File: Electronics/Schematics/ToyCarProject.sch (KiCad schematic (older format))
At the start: 24 parts

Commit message: Project Schematics update
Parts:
- added P?: MSP430G2553, symbol MSP430G2553
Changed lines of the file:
@@
-EESchema Schematic File Version 2  date 25/02/2013 10:51:28
+EESchema Schematic File Version 2  date 2/28/2013 14:46:19
 LIBS:power
 LIBS:device
@@
 LIBS:contrib
 LIBS:valves
-EELAYER 43  0
+LIBS:ToyCarProject-cache
+EELAYER 27 0
 EELAYER END
-$Descr A4 11700 8267
+$Descr A4 11693 8268
 encoding utf-8
 Sheet 1 1
 Title ""
-Date "25 feb 2013"
+Date "28 feb 2013"
 Rev ""
 Comp ""
@@
 F 0 "V?" H 4150 1450 50  0000 L CNN
 F 1 "BAT" H 4150 1250 50  0000 L CNN
+F 2 "" H 4100 1350 60  0001 C CNN
+F 3 "" H 4100 1350 60  0001 C CNN
 	1    4100 1350
 	1    0    0    -1
@@
 F 0 "U?" H 4950 1104 60  0000 C CNN
 F 1 "LD1117S33" H 4800 1500 60  0000 C CNN
+F 2 "" H 4800 1300 60  0001 C CNN
+F 3 "" H 4800 1300 60  0001 C CNN
 	1    4800 1300
 	1    0    0    -1
@@
 F 0 "R?" V 2830 1800 50  0000 C CNN
 F 1 "470" V 2750 1800 50  0000 C CNN
+F 2 "" H 2750 1800 60  0001 C CNN
+F 3 "" H 2750 1800 60  0001 C CNN
 	1    2750 1800
 	-1   0    0    1
@@
 F 0 "R?" V 2480 1800 50  0000 C CNN
 F 1 "470" V 2400 1800 50  0000 C CNN
+F 2 "" H 2400 1800 60  0001 C CNN
+F 3 "" H 2400 1800 60  0001 C CNN
 	1    2400 1800
 	-1   0    0    1
@@
 F 0 "R?" V 2130 1800 50  0000 C CNN
 F 1 "470" V 2050 1800 50  0000 C CNN
+F 2 "" H 2050 1800 60  0001 C CNN
+F 3 "" H 2050 1800 60  0001 C CNN
 	1    2050 1800
 	-1   0    0    1
@@
 F 0 "D?" H 2750 1450 50  0000 C CNN
 F 1 "Mbed LED" H 2750 1250 50  0000 C CNN
+F 2 "" H 2750 1350 60  0001 C CNN
+F 3 "" H 2750 1350 60  0001 C CNN
 	1    2750 1350
 	0    -1   -1   0
@@
 F 0 "D?" H 2400 1450 50  0000 C CNN
 F 1 "Mbed LED" H 2400 1250 50  0000 C CNN
+F 2 "" H 2400 1350 60  0001 C CNN
+F 3 "" H 2400 1350 60  0001 C CNN
 	1    2400 1350
 	0    -1   -1   0
@@
 F 0 "D?" H 2050 1450 50  0000 C CNN
 F 1 "Mbed LED" H 2050 1250 50  0000 C CNN
+F 2 "" H 2050 1350 60  0001 C CNN
+F 3 "" H 2050 1350 60  0001 C CNN
 	1    2050 1350
 	0    -1   -1   0
@@
 F 0 "L?" V 9750 1400 40  0000 C CNN
 F 1 "INDUCTOR" V 9900 1400 40  0000 C CNN
+F 2 "" H 9800 1400 60  0001 C CNN
+F 3 "" H 9800 1400 60  0001 C CNN
 	1    9800 1400
 	0    -1   -1   0
@@
 F 0 "L?" V 9150 1400 40  0000 C CNN
 F 1 "INDUCTOR" V 9300 1400 40  0000 C CNN
+F 2 "" H 9200 1400 60  0001 C CNN
+F 3 "" H 9200 1400 60  0001 C CNN
 	1    9200 1400
 	0    -1   -1   0
@@
 F 0 "#PWR?" H 9500 1350 20  0001 C CNN
 F 1 "+BAT_CAR" H 9500 1500 30  0000 C CNN
+F 2 "" H 9500 1400 60  0001 C CNN
+F 3 "" H 9500 1400 60  0001 C CNN
 	1    9500 1400
 	1    0    0    -1
@@
 F 0 "Q?" H 8800 1450 50  0000 R CNN
 F 1 "NPN" H 8650 1450 50  0000 R CNN
+F 2 "" H 8800 1600 60  0001 C CNN
+F 3 "" H 8800 1600 60  0001 C CNN
 	1    8800 1600
 	1    0    0    -1
@@
 F 0 "Q?" H 10200 1450 50  0000 R CNN
 F 1 "NPN" H 10050 1450 50  0000 R CNN
+F 2 "" H 10200 1600 60  0001 C CNN
+F 3 "" H 10200 1600 60  0001 C CNN
 	1    10200 1600
 	-1   0    0    -1
@@
 F 0 "#PWR?" H 9500 1800 30  0001 C CNN
 F 1 "GND" H 9500 1730 30  0001 C CNN
+F 2 "" H 9500 1800 60  0001 C CNN
+F 3 "" H 9500 1800 60  0001 C CNN
 	1    9500 1800
 	1    0    0    -1
@@
 F 0 "R?" V 7830 1600 50  0000 C CNN
 F 1 "750" V 7750 1600 50  0000 C CNN
+F 2 "" H 7750 1600 60  0001 C CNN
+F 3 "" H 7750 1600 60  0001 C CNN
 	1    7750 1600
 	0    -1   -1   0
@@
 F 0 "R?" V 7830 1950 50  0000 C CNN
 F 1 "750" V 7750 1950 50  0000 C CNN
+F 2 "" H 7750 1950 60  0001 C CNN
+F 3 "" H 7750 1950 60  0001 C CNN
 	1    7750 1950
 	0    -1   -1   0
@@
 F 0 "R?" V 9630 3700 50  0000 C CNN
 F 1 "0" V 9550 3700 50  0000 C CNN
+F 2 "" H 9550 3700 60  0001 C CNN
+F 3 "" H 9550 3700 60  0001 C CNN
 	1    9550 3700
 	0    -1   -1   0
@@
 F 0 "R?" V 7830 4350 50  0000 C CNN
 F 1 "750" V 7750 4350 50  0000 C CNN
+F 2 "" H 7750 4350 60  0001 C CNN
+F 3 "" H 7750 4350 60  0001 C CNN
 	1    7750 4350
 	0    -1   -1   0
@@
 F 0 "R?" V 7830 4000 50  0000 C CNN
 F 1 "750" V 7750 4000 50  0000 C CNN
+F 2 "" H 7750 4000 60  0001 C CNN
+F 3 "" H 7750 4000 60  0001 C CNN
 	1    7750 4000
 	0    -1   -1   0
@@
 F 0 "R?" V 8680 3400 50  0000 C CNN
 F 1 "RPNP" V 8600 3400 50  0000 C CNN
+F 2 "" H 8600 3400 60  0001 C CNN
+F 3 "" H 8600 3400 60  0001 C CNN
 	1    8600 3400
 	-1   0    0    1
@@
 F 0 "R?" V 10430 3400 50  0000 C CNN
 F 1 "RPNP" V 10350 3400 50  0000 C CNN
+F 2 "" H 10350 3400 60  0001 C CNN
+F 3 "" H 10350 3400 60  0001 C CNN
 	1    10350 3400
 	1    0    0    -1
@@
 F 0 "#PWR?" H 9500 4200 30  0001 C CNN
 F 1 "GND" H 9500 4130 30  0001 C CNN
+F 2 "" H 9500 4200 60  0001 C CNN
+F 3 "" H 9500 4200 60  0001 C CNN
 	1    9500 4200
 	1    0    0    -1
@@
 F 0 "#PWR?" H 9500 2550 20  0001 C CNN
 F 1 "+BAT_CAR" H 9500 2700 30  0000 C CNN
+F 2 "" H 9500 2600 60  0001 C CNN
+F 3 "" H 9500 2600 60  0001 C CNN
 	1    9500 2600
 	1    0    0    -1
@@
 F 0 "M" V 9700 3100 70  0000 C CNN
 F 1 "M" V 9700 3150 70  0000 C CNN
+F 2 "" H 9500 3100 60  0001 C CNN
+F 3 "" H 9500 3100 60  0001 C CNN
 	1    9500 3100
 	0    -1   -1   0
@@
 F 0 "Q?" H 9950 3000 60  0000 R CNN
 F 1 "PNP" H 9800 3000 60  0000 R CNN
+F 2 "" H 9950 3150 60  0001 C CNN
+F 3 "" H 9950 3150 60  0001 C CNN
 	1    9950 3150
 	-1   0    0    1
@@
 F 0 "Q?" H 9050 3000 60  0000 R CNN
 F 1 "PNP" H 8900 3000 60  0000 R CNN
+F 2 "" H 9050 3150 60  0001 C CNN
+F 3 "" H 9050 3150 60  0001 C CNN
 	1    9050 3150
 	1    0    0    1
@@
 F 0 "Q?" H 9950 3850 50  0000 R CNN
 F 1 "NPN" H 9800 3850 50  0000 R CNN
+F 2 "" H 9950 4000 60  0001 C CNN
+F 3 "" H 9950 4000 60  0001 C CNN
 	1    9950 4000
 	-1   0    0    -1
@@
 F 0 "Q?" H 9050 3850 50  0000 R CNN
 F 1 "NPN" H 8900 3850 50  0000 R CNN
+F 2 "" H 9050 4000 60  0001 C CNN
+F 3 "" H 9050 4000 60  0001 C CNN
 	1    9050 4000
 	1    0    0    -1
 $EndComp
+$Comp
+L MSP430G2553 P?
+U 1 1 512F700D
+P 5000 3350
+F 0 "P?" H 4950 3950 70  0000 C CNN
+F 1 "MSP430G2553" H 5000 2750 70  0000 C CNN
+F 2 "" H 5000 3350 60  0000 C CNN
+F 3 "" H 5000 3350 60  0000 C CNN
+	1    5000 3350
+	1    0    0    -1
+$EndComp

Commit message: Project Schematic Update
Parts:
- removed U?: LD1117S33, symbol LM7805
- removed V?: BAT, symbol BAT
- added BT?: BATTERY_Front, symbol BATTERY
- added BT?: BATTERY_Top, symbol BATTERY
- added D?: LED, symbol LED
- added P?: A2080, symbol A2080
- added P?: PC, symbol CONN_6
- added R?: ?, symbol R
- added SP?: SPEAKER, symbol SPEAKER
- R? (x4): value 750 -> 350
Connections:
- net +BAT_CAR: now also P?.1 (VCC), BT?.1 (+), BT?.1 (+), P?.2, P?.4 (VDDIO), P?.8 (VDDA), R?.1
- net GND: now also D?.2 (K), D?.2 (K), D?.2 (K), P?.20 (GND), BT?.2 (-), BT?.2 (-), P?.5, P?.6 (GND), SP?.1
- net at Q?.2 (B): now also R?.1; no longer R?.2
- net at Q?.2 (B), R?.2: now also R?.1; no longer R?.2
- net at R?.1: now also Q?.2 (B) (x2)
- net at R?.2: now also P?.5 (P1.3); no longer Q?.2 (B)
- net at R?.2: now also P?.6 (P1.4); no longer Q?.2 (B)
- net at R?.1: now also P?.13 (P2.5/TA1.2)
- net at R?.1: now also P?.12 (P2.4/TA1.2)
- net at R?.1: now also P?.11 (P2.3/TA1.0)
- net at P?.10 (P2.2/TA1.1): now also R?.2
- net at P?.14 (P1.6/SOMI): now also P?.15 (P1.7/SIMO), P?.1 (SDIO)
- net Link_Rst: now reaches P?.16 (Rst)
- net Link_Rst: now also P?.4
- net Link_Test: now reaches P?.17 (Test)
- net Link_Test: now also P?.3
- net at P?.19 (P2.6/TA0.1): now also SP?.2
- net Link_RX: now reaches P?.3 (P1.1/RX)
- net Link_RX: now also P?.1
- net Link_TX: now reaches P?.4 (P1.2/TX)
- net Link_TX: now also P?.6
- net at P?.7 (P1.5/SPICLK): now also P?.5 (SCLK)
- net at P?.9 (P2.1/TA1.1): now also R?.2
- new net: D?.1 (A), P?.3 (Motion)
- new net: D?.2 (K), R?.2
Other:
- note added: "Mouse Tracking"
- moved on the sheet: D?, L?, M, P?, Q?, R?

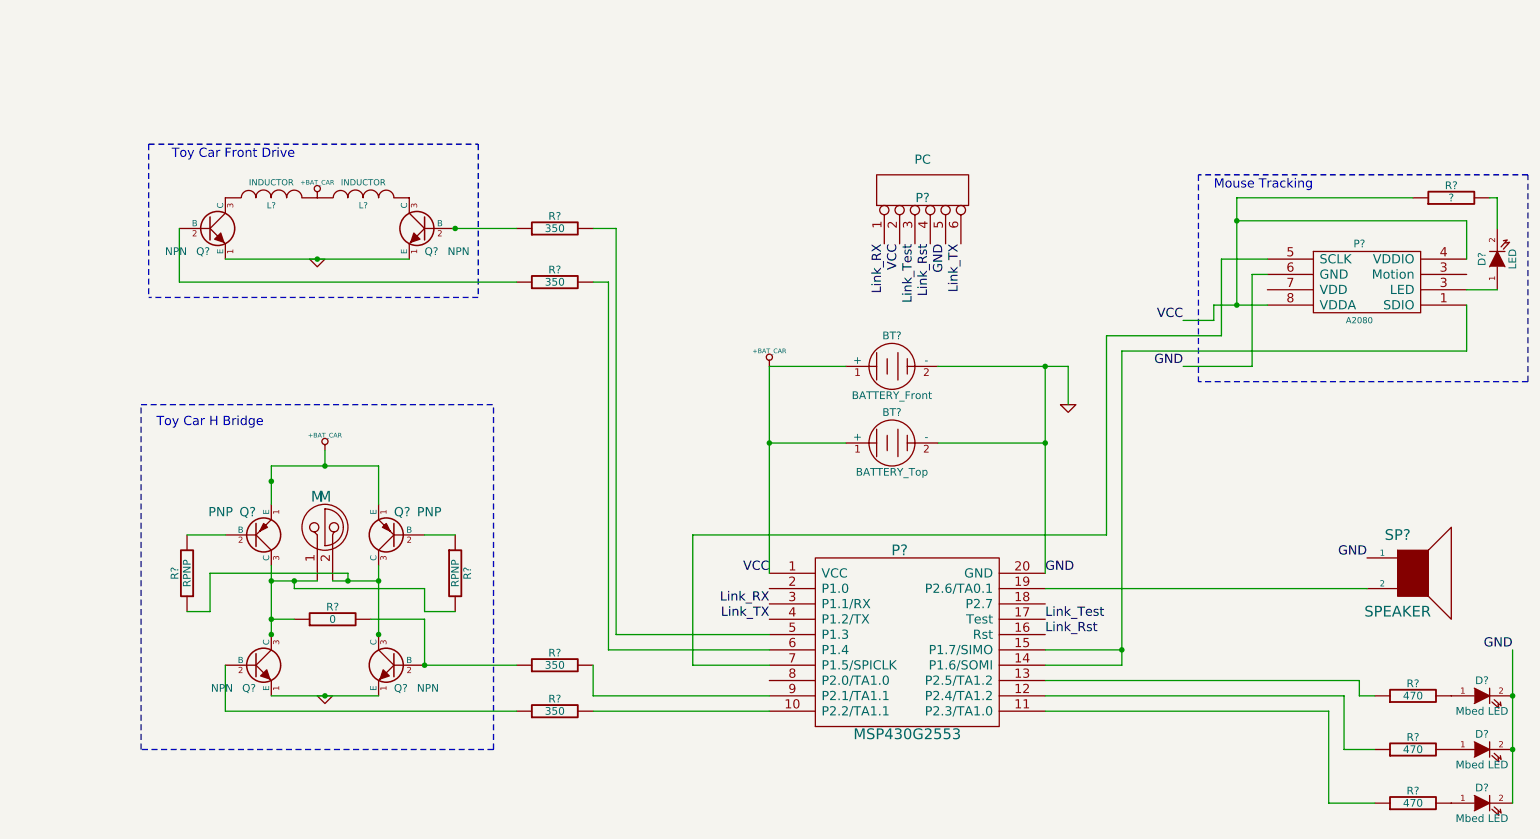
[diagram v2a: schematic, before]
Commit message: New schematics with voltage regulator ( 4 battery-element powered. )
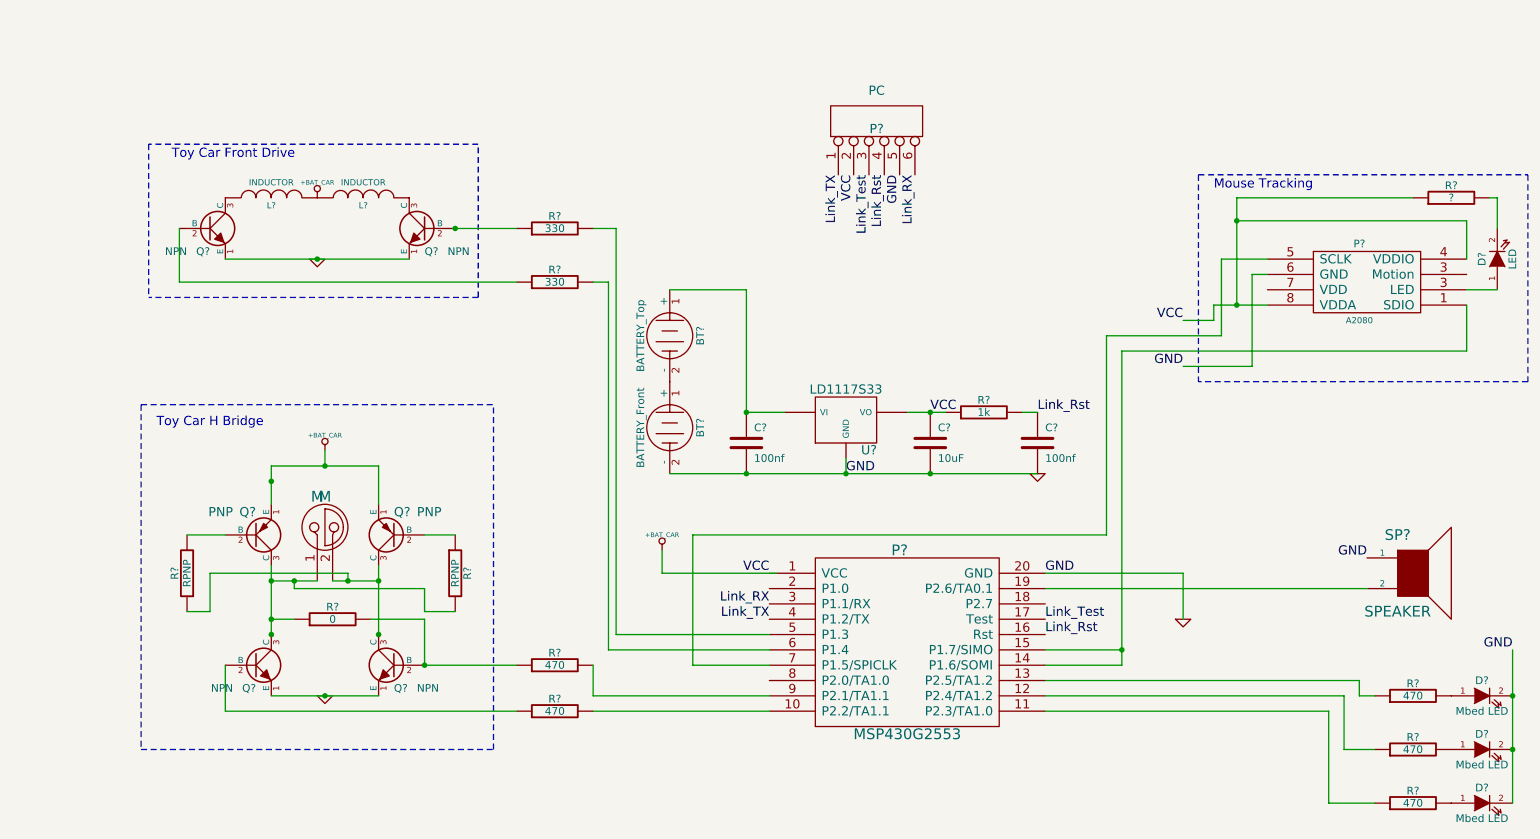
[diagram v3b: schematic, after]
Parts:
- added C? (x2): 100nf, symbol C
- added C?: 10uF, symbol C
- added R?: 1k, symbol R
- added U?: LD1117S33, symbol 7805
- R? (x2): value 350 -> 470
- R? (x2): value 350 -> 330
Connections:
- net +BAT_CAR: now also C?.1, R?.1, U?.VO; no longer BT?.1 (+), BT?.1 (+)
- net GND: now also C?.2, C?.2, C?.2, U?.GND; no longer BT?.2 (-)
- net Link_RX: now also P?.6; no longer P?.1
- net Link_Rst: now also C?.1, R?.2
- net Link_TX: now also P?.1; no longer P?.6
- net at P?.3 (Motion): now also D?.1 (A)
- new net: BT?.1 (+), BT?.2 (-)
- new net: BT?.1 (+), C?.1, U?.VI
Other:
- moved on the sheet: BT?, P?

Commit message: Update to the schematics after the change in power setup ( battery connection )
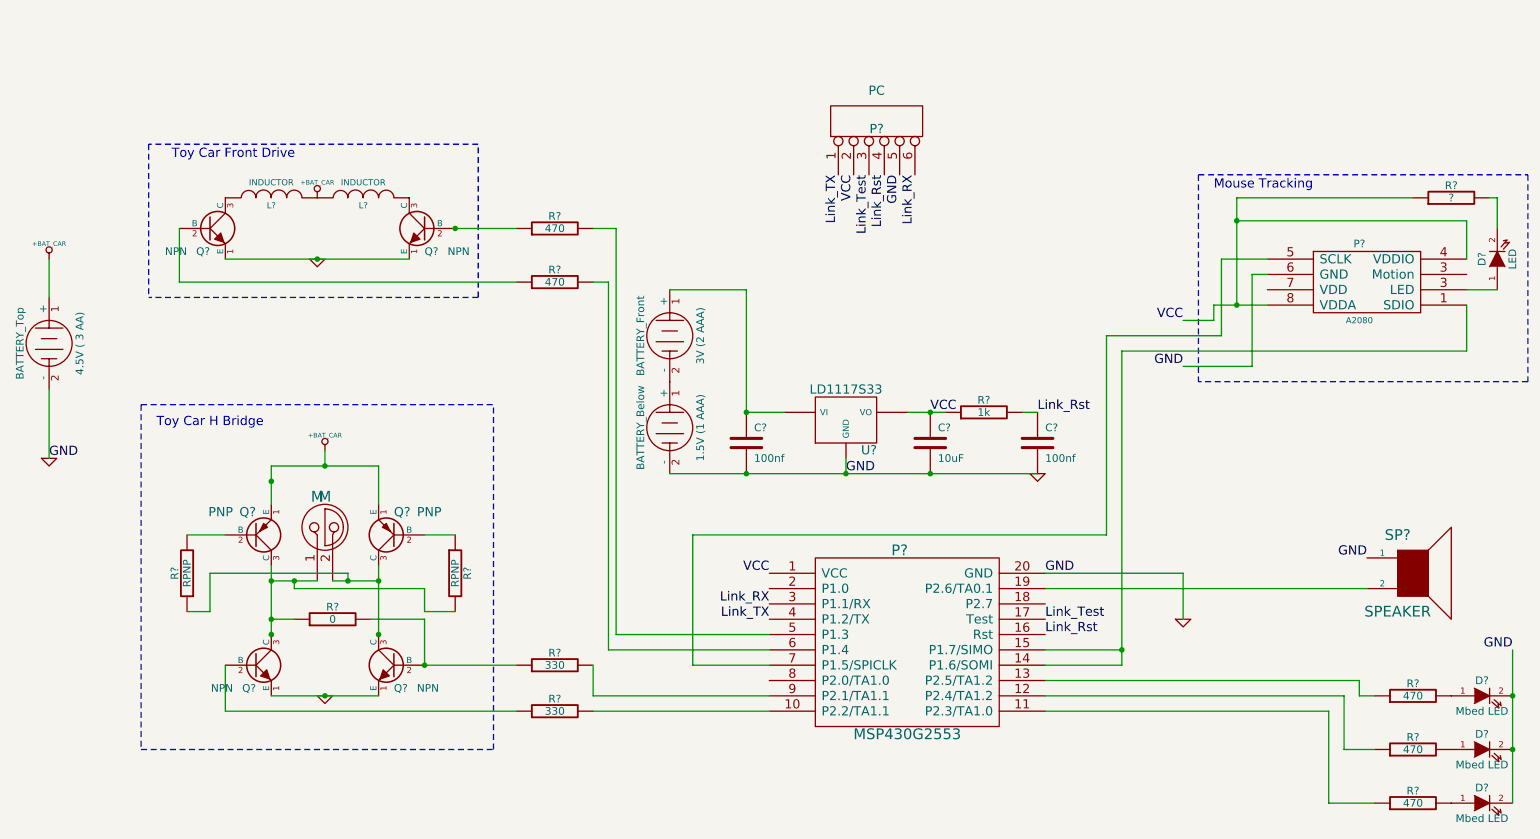
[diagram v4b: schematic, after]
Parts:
- added 3V: BATTERY_Front, symbol BATTERY
- 1.5V: renamed from BT?; value BATTERY_Front -> BATTERY_Below
- R? (x2): value 470 -> 330
- R? (x2): value 330 -> 470
- gave numbers to parts that had none: 1
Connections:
- net +BAT_CAR: now also 4.5V.1 (+); no longer C?.1, P?.1 (VCC), P?.2, P?.4 (VDDIO), P?.8 (VDDA), R?.1, R?.1, U?.VO
- net GND: now also 4.5V.2 (-)
- net at P?.3 (Motion): now also D?.1 (A)
- net at 1.5V.1 (+): now also 3V.2 (-); no longer 4.5V.2 (-)
- net at C?.1, U?.VI: now also 3V.1 (+); no longer 4.5V.1 (+)
- new net VCC: C?.1, P?.1 (VCC), P?.2, P?.4 (VDDIO), P?.8 (VDDA), R?.1, R?.1, U?.VO
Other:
- moved on the sheet: 4.5V ( 3 AA)
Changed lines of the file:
@@
-EESchema Schematic File Version 2  date 18/03/2013 15:27:28
+EESchema Schematic File Version 2  date 07/05/2013 16:46:18
 LIBS:power
 LIBS:device
@@
 Sheet 1 1
 Title ""
-Date "18 mar 2013"
+Date "7 may 2013"
 Rev ""
 Comp ""
@@
 Comment4 ""
 $EndDescr
-Text Label 6300 4050 0    60   ~ 0
+Text Label 1100 3950 0    60   ~ 0
 GND
+Wire Wire Line
+	1100 3950 1100 3500
 Connection ~ 6850 4050
 Wire Wire Line
-	7550 4050 5150 4050
+	5150 4050 5650 4050
+Wire Wire Line
+	5650 4050 6300 4050
+Wire Wire Line
+	6300 4050 6850 4050
+Wire Wire Line
+	6850 4050 7550 4050
 Connection ~ 6850 3650
 Wire Wire Line
-	6950 3650 6700 3650
+	6700 3650 6850 3650
+Wire Wire Line
+	6850 3650 6950 3650
 Connection ~ 6300 4050
 Wire Wire Line
@@
 	5900 3650 5650 3650
 Wire Wire Line
-	5100 4550 5100 4700
-Wire Wire Line
-	5100 4700 5850 4700
-Wire Wire Line
 	7600 4800 9700 4800
 Connection ~ 10650 5500
 Wire Wire Line
-	10650 5200 10650 6200
+	10650 6200 10650 5850
+Wire Wire Line
+	10650 5850 10650 5500
+Wire Wire Line
+	10650 5500 10650 5200
 Wire Wire Line
 	9750 6200 9450 6200
@@
 	7600 5300 8100 5300
 Wire Wire Line
-	8100 5300 8100 3250
+	8100 5300 8100 5200
+Wire Wire Line
+	8100 5200 8100 3250
 Wire Wire Line
 	8100 3250 10350 3250
@@
 	8700 3050 8700 2950
 Wire Wire Line
-	8700 2950 9050 2950
+	8700 2950 8850 2950
+Wire Wire Line
+	8850 2950 9050 2950
 Wire Wire Line
 	8750 2650 8750 3150
@@
 	10000 2250 8850 2250
 Wire Wire Line
-	8850 2250 8850 2950
+	8850 2250 8850 2400
+Wire Wire Line
+	8850 2400 8850 2950
 Wire Wire Line
 	10500 2250 10550 2250
@@
 	3550 4950 3750 4950
 Wire Wire Line
-	2550 5100 2550 4650
+	2550 4650 2550 4750
+Wire Wire Line
+	2550 4750 2550 5000
+Wire Wire Line
+	2550 5000 2550 5100
 Connection ~ 2550 4100
 Wire Wire Line
@@
 	3550 5000 3200 5000
 Wire Wire Line
-	2550 4250 2550 4000
-Wire Wire Line
-	2550 4000 3250 4000
+	2550 4250 2550 4100
+Wire Wire Line
+	2550 4100 2550 4000
+Wire Wire Line
+	2550 4000 2900 4000
+Wire Wire Line
+	2900 4000 3250 4000
 Wire Wire Line
 	3250 4000 3250 4250
 Wire Wire Line
-	3250 5500 2550 5500
+	2550 5500 2900 5500
+Wire Wire Line
+	2900 5500 3250 5500
 Connection ~ 2900 5500
 Wire Wire Line
-	2550 4750 2850 4750
+	2850 4750 2700 4750
+Wire Wire Line
+	2700 4750 2550 4750
 Connection ~ 2550 4750
 Wire Wire Line
-	2950 4750 3250 4750
+	2950 4750 3050 4750
+Wire Wire Line
+	3050 4750 3250 4750
 Connection ~ 3250 4750
 Wire Wire Line
@@
 Connection ~ 3050 4750
 Wire Wire Line
-	3250 5100 3250 4650
+	3250 4650 3250 4750
+Wire Wire Line
+	3250 4750 3250 5100
 Wire Notes Line
 	1700 3600 1700 5850
@@
 Connection ~ 2850 2650
 Wire Wire Line
-	3450 2650 2250 2650
+	2250 2650 2850 2650
+Wire Wire Line
+	2850 2650 3450 2650
 Wire Notes Line
 	3900 2900 1750 2900
@@
 Wire Wire Line
 	7450 3650 7550 3650
+Wire Wire Line
+	1100 2650 1100 2900
+$Comp
+L GND #PWR?
+U 1 1 51892109
+P 1100 3950
+F 0 "#PWR?" H 1100 3950 30  0001 C CNN
+F 1 "GND" H 1100 3880 30  0001 C CNN
+	1    1100 3950
+	1    0    0    -1
+$EndComp
+$Comp
+L BATTERY 3V
+U 1 1 518920D5
+P 5150 3150
+F 0 "3V (2 AAA)" H 5150 3350 50  0000 C CNN
+F 1 "BATTERY_Front" H 5150 2960 50  0000 C CNN
+	1    5150 3150
+	0    1    1    0
+$EndComp
+$Comp
+L +BAT_CAR #PWR?
+U 1 1 513C68E2
+P 1100 2650
+F 0 "#PWR?" H 1100 2600 20  0001 C CNN
+F 1 "+BAT_CAR" H 1100 2750 30  0000 C CNN
+	1    1100 2650
+	1    0    0    -1
+$EndComp
+Text Label 6300 4050 0    60   ~ 0
+GND
 Text Label 7550 3650 0    60   ~ 0
 Link_Rst
@@
 $EndComp
 $Comp
-L +BAT_CAR #PWR?
-U 1 1 513C68E2
-P 5100 4550
-F 0 "#PWR?" H 5100 4500 20  0001 C CNN
-F 1 "+BAT_CAR" H 5100 4650 30  0000 C CNN
-	1    5100 4550
-	1    0    0    -1
-$EndComp
-$Comp
 L GND #PWR?
 U 1 1 513C68E8
@@
 $EndComp
 $Comp
-L BATTERY BT?
+L BATTERY 4.5V
 U 1 1 513C688D
-P 5150 3150
-F 0 "BT?" H 5150 3350 50  0000 C CNN
-F 1 "BATTERY_Top" H 5150 2960 50  0000 C CNN
-	1    5150 3150
+P 1100 3200
+F 0 "4.5V ( 3 AA)" H 1100 3400 50  0000 C CNN
+F 1 "BATTERY_Top" H 1100 3010 50  0000 C CNN
+	1    1100 3200
 	0    1    1    0
 $EndComp
 $Comp
-L BATTERY BT?
+L BATTERY 1.5V
 U 1 1 513C6889
 P 5150 3750
-F 0 "BT?" H 5150 3950 50  0000 C CNN
-F 1 "BATTERY_Front" H 5150 3560 50  0000 C CNN
+F 0 "1.5V (1 AAA)" H 5150 3950 50  0000 C CNN
+F 1 "BATTERY_Below" H 5150 3560 50  0000 C CNN
 	1    5150 3750
 	0    1    1    0
@@
 P 4400 2800
 F 0 "R?" V 4480 2800 50  0000 C CNN
-F 1 "330" V 4400 2800 50  0000 C CNN
+F 1 "470" V 4400 2800 50  0000 C CNN
 	1    4400 2800
 	0    -1   -1   0
@@
 P 4400 2450
 F 0 "R?" V 4480 2450 50  0000 C CNN
-F 1 "330" V 4400 2450 50  0000 C CNN
+F 1 "470" V 4400 2450 50  0000 C CNN
 	1    4400 2450
 	0    -1   -1   0
@@
 P 4400 5600
 F 0 "R?" V 4480 5600 50  0000 C CNN
-F 1 "470" V 4400 5600 50  0000 C CNN
+F 1 "330" V 4400 5600 50  0000 C CNN
 	1    4400 5600
 	0    -1   -1   0
@@
 P 4400 5300
 F 0 "R?" V 4480 5300 50  0000 C CNN
-F 1 "470" V 4400 5300 50  0000 C CNN
+F 1 "330" V 4400 5300 50  0000 C CNN
 	1    4400 5300
 	0    -1   -1   0
